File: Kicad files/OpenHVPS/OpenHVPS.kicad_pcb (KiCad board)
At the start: 2 copper layers, 36 x 36 mm, 64 parts, among them J1 Conn_01x03_Male, Q1 FQT7N10, Q2 BC846, Q3 MMDT3906, U1 74HC14, U2 MAX4162, U3 CD14538BM, U4 MAX6008AEUR+T

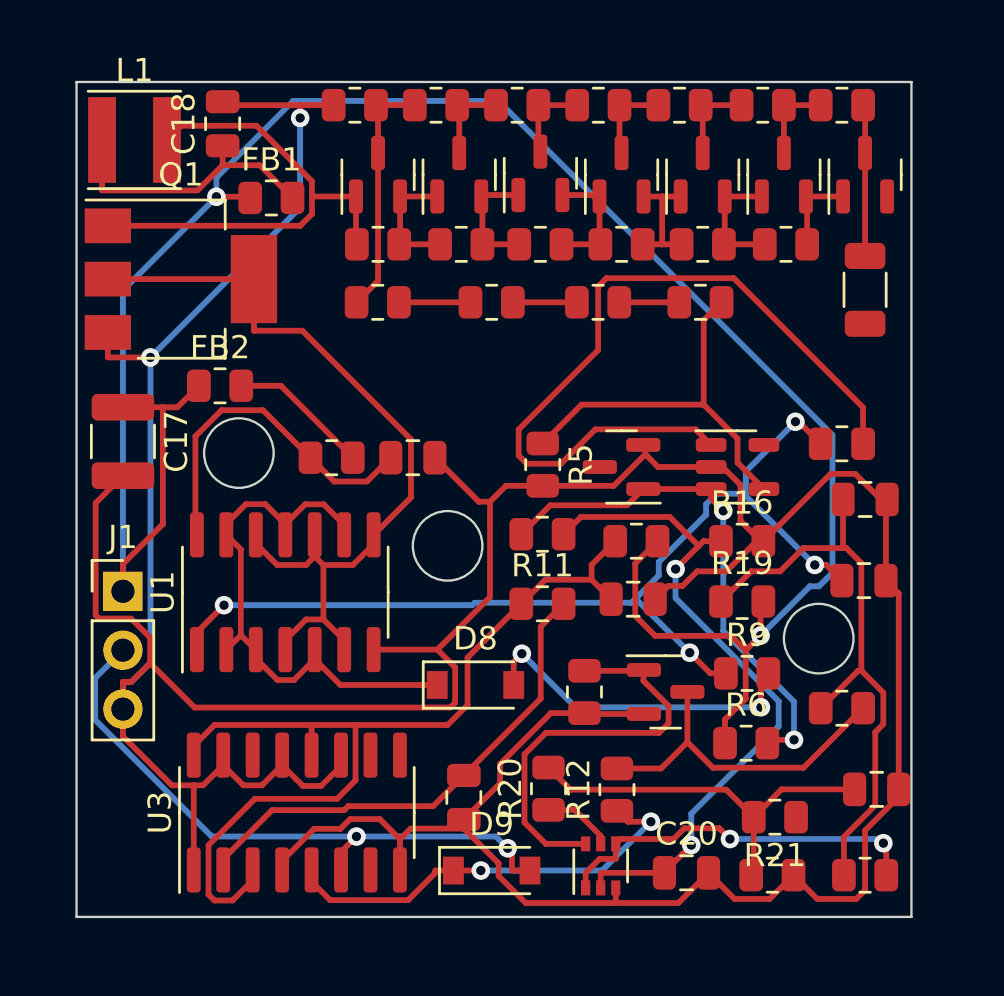
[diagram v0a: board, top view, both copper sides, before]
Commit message: Updated board with fill areas
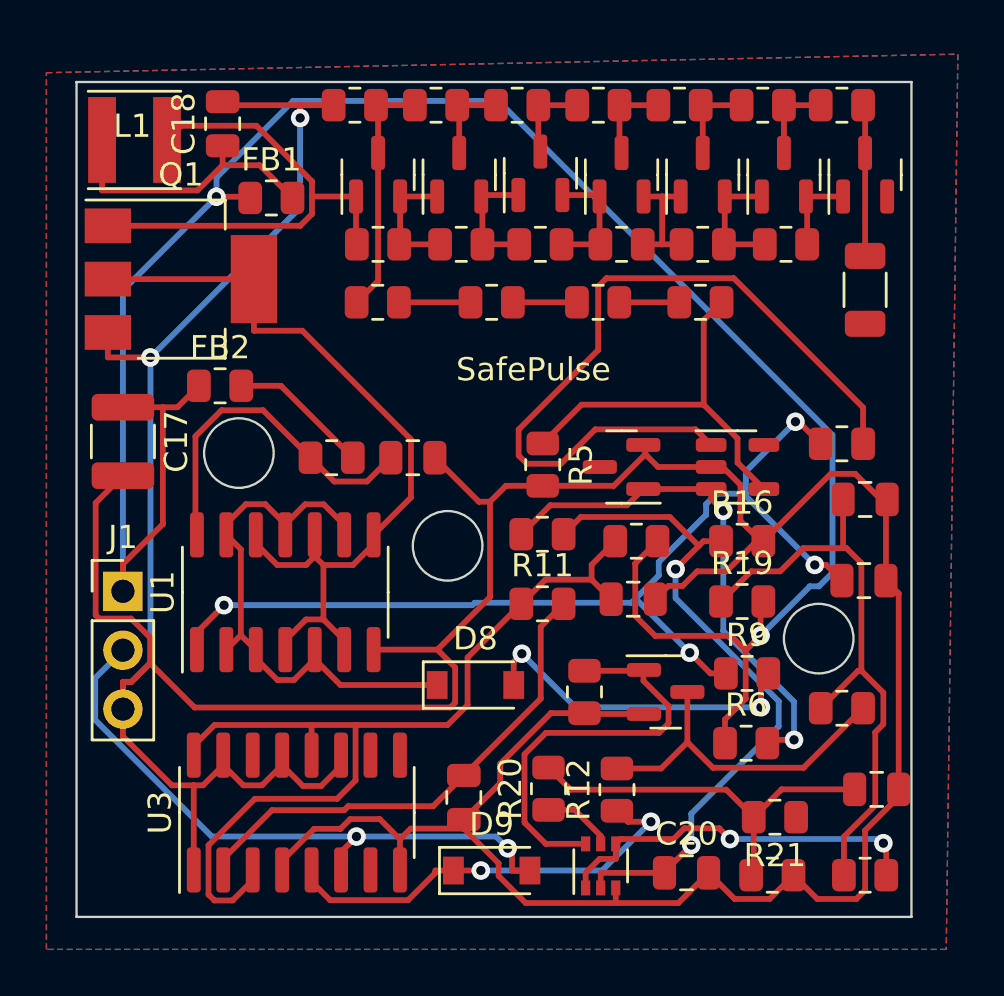
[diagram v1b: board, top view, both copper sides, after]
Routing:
- added copper zone on B.Cu, net GND
- added copper zone on F.Cu, net GND
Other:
- board text added: "SafePulse"

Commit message: Tested new layout board
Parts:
- moved C21 13.0 mm to (128.7, 93.9), turned to 90 degrees
- moved R18 11.7 mm to (123.1, 93.9), turned to 90 degrees
- moved R19 11.1 mm to (128.8, 97.5), turned to 90 degrees
- moved C22 8.65 mm to (125.9, 93.9), turned to 90 degrees
- moved R9 8.42 mm to (131.5, 97.5), turned to 90 degrees
- moved FB2 8.34 mm to (107.0, 68.8)
- moved D9 7.89 mm to (116.2, 90.3), turned to 180 degrees
- moved U4 7.42 mm to (126.7, 73.9)
- moved R5 7.42 mm to (123.5, 73.9), turned to 90 degrees
- moved R21 7.14 mm to (123.2, 97.5), turned to -90 degrees
- moved U2 7.12 mm to (130.9, 73.9)
- moved Q3 6.77 mm to (116.8, 94.3)
- moved C16 6.65 mm to (121.6, 90.3), turned to 180 degrees
- moved R10 6.20 mm to (110.8, 74.0), turned to 90 degrees
- moved C20 5.93 mm to (120.4, 97.5), turned to 90 degrees
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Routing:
- net GND: track 187.2 -> 0.00 mm, vias 2 -> 0
- net +3V3: track 93.1 -> 0.00 mm, vias 2 -> 0
- net Net-(C14-Pad1): track 43.9 -> 0.00 mm, vias 4 -> 0
- net Net-(C19-Pad1): track 41.1 -> 0.00 mm
- net Net-(Q1-Pad2): track 36.3 -> 0.00 mm
- net Net-(R8-Pad2): track 33.5 -> 0.00 mm
- net Net-(C20-Pad1): track 29.5 -> 0.00 mm, vias 2 -> 0
- net Net-(D9-Pad2): track 27.1 -> 0.00 mm, vias 2 -> 0
- net Net-(C21-Pad1): track 26.3 -> 0.00 mm
- net Net-(D8-Pad1): track 24.1 -> 0.00 mm
- net +2V5: track 22.5 -> 0.00 mm, vias 2 -> 0
- net Net-(C2-Pad1): track 21.9 -> 0.00 mm
- net Net-(C16-Pad1): track 21.5 -> 0.00 mm
- net Net-(D9-Pad1): track 18.6 -> 0.00 mm, vias 2 -> 0
- net Net-(Q2-Pad1): track 18.0 -> 0.00 mm
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
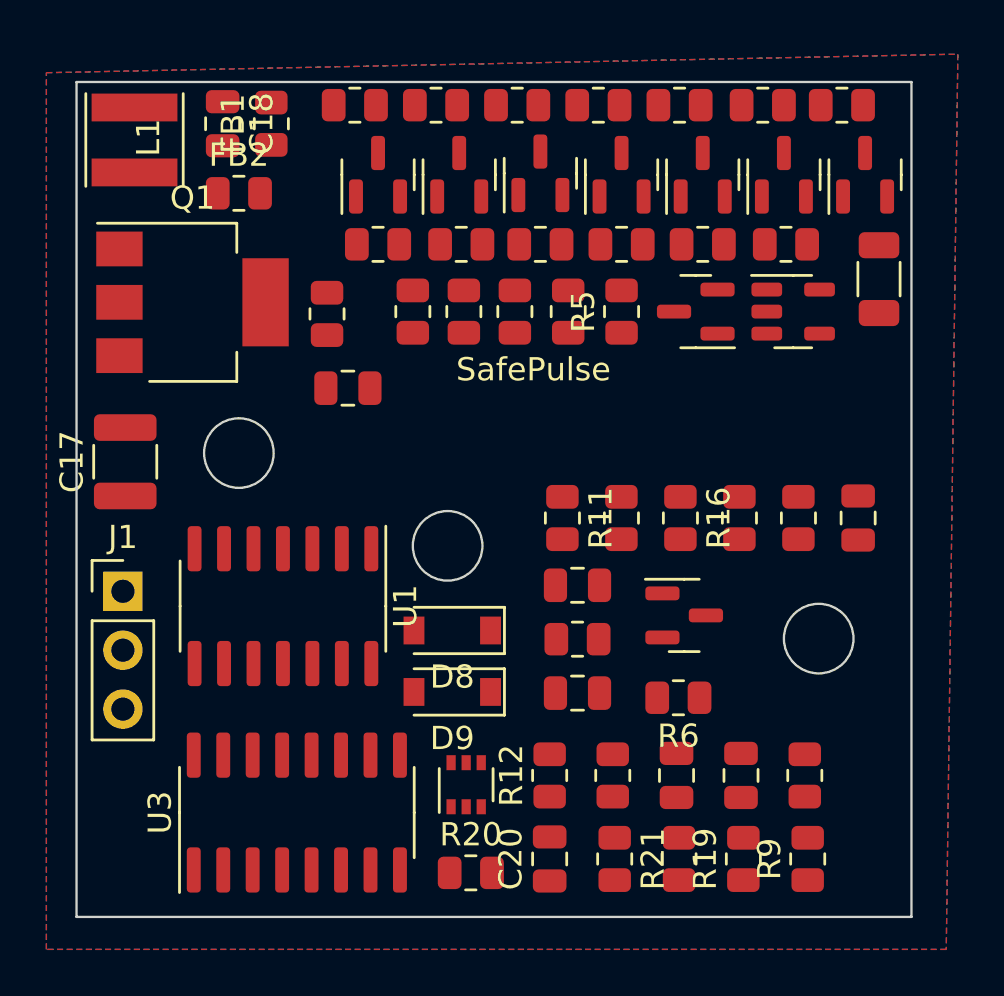
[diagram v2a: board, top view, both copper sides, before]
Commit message: Round conners and less vias. Space around holes
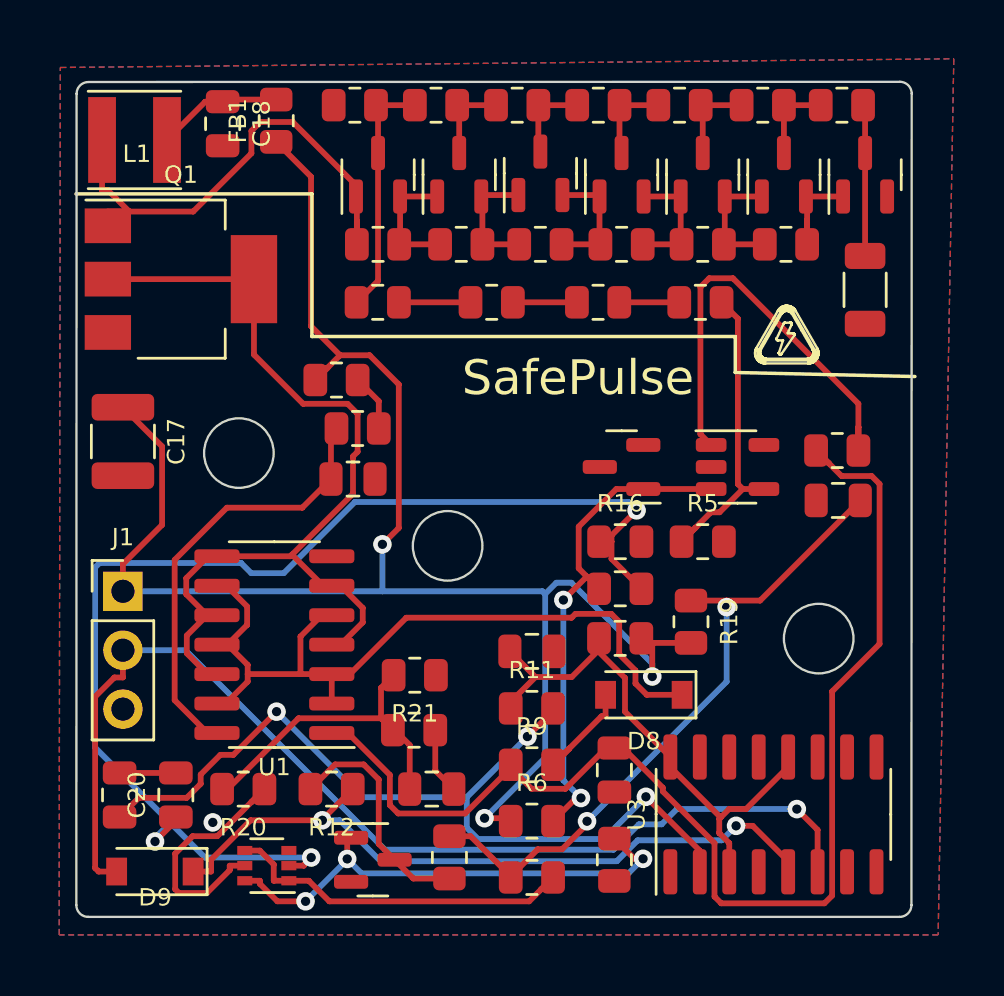
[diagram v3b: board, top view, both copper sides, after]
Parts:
- moved U3 20.5 mm to (130.0, 95.6)
- moved C16 20.2 mm to (101.9, 94.7), turned to 90 degrees
- moved Q2 17.1 mm to (112.8, 97.5)
- moved C20 16.4 mm to (104.3, 94.7)
- moved R14 15.7 mm to (116.1, 97.4), turned to -90 degrees
- moved C14 15.1 mm to (123.2, 93.7)
- moved D9 15.0 mm to (103.4, 98.0)
- moved R22 12.7 mm to (114.6, 91.9), turned to 0 degrees
- moved C21 12.6 mm to (132.8, 82.0), turned to 180 degrees
- moved R9 12.6 mm to (119.6, 93.4), turned to 0 degrees
- moved R21 11.7 mm to (114.6, 89.6), turned to 180 degrees
- moved C22 10.6 mm to (115.3, 94.5), turned to 0 degrees
- moved R5 10.5 mm to (127.0, 83.8), turned to 0 degrees
- moved R19 10.5 mm to (126.5, 87.3), turned to -90 degrees
- moved R20 10.5 mm to (107.2, 94.5), turned to 180 degrees
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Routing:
- net +3V3: track 0.00 -> 75.0 mm, vias 0 -> 3
- net Net-(C14-Pad1): track 0.00 -> 53.0 mm
- net Net-(C20-Pad1): track 0.00 -> 52.6 mm, vias 0 -> 3
- net Net-(D9-Pad2): track 0.00 -> 47.5 mm, vias 0 -> 1
- net Net-(Q1-Pad2): track 0.00 -> 39.8 mm
- net Net-(C16-Pad1): track 0.00 -> 38.2 mm, vias 0 -> 3
- net Net-(D8-Pad1): track 0.00 -> 34.8 mm
- net Net-(D9-Pad1): track 0.00 -> 31.2 mm, vias 0 -> 2
- net Net-(C21-Pad1): track 0.00 -> 28.9 mm, vias 0 -> 2
- net Net-(C19-Pad1): track 0.00 -> 23.6 mm
- net Net-(C2-Pad1): track 0.00 -> 21.9 mm
- net Net-(Q2-Pad1): track 0.00 -> 21.5 mm, vias 0 -> 3
- net +2V5: track 0.00 -> 21.3 mm, vias 0 -> 2
- net Net-(R8-Pad2): track 0.00 -> 19.2 mm
- net Net-(C15-Pad1): track 0.00 -> 18.9 mm
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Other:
- outline, holes or cut-outs redrawn

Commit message: version 2 of the SafePulse
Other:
- board text added: "+3.3V"
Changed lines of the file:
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@@
     (effects (font (size 1.5 1.5) (thickness 0.15)))
+  )
+  (gr_text "+3.3V" (at 103.69 85.88 270) (layer "F.SilkS")
+    (effects (font (size 0.5 0.5) (thickness 0.1)))
+  )
+  (gr_text "+3.3V" (at 103.74 88.42 270) (layer "F.SilkS")
+    (effects (font (size 0.5 0.5) (thickness 0.1)))
+  )
+  (gr_text "+3.3V" (at 103.76 91.13 270) (layer "F.SilkS")
+    (effects (font (size 0.5 0.5) (thickness 0.1)))
   )
   (segment (start 113 67.0625) (end 113 72.5755) (width 0.25) (layer "F.Cu") (net 1))
